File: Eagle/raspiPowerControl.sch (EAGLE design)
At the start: 10 parts, among them Q1 FDN360P, T1 BC847

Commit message: Update Eagle
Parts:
- added C3: 100n, rcl:C-EUC0805
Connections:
- net +5V: now also C3.2
- net GND: now also C3.1
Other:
- moved on the sheet: +5V, GND, R1
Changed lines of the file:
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@@
 <part name="C1" library="rcl" library_urn="urn:adsk.eagle:library:334" deviceset="C-EU" device="C0805" package3d_urn="urn:adsk.eagle:package:23617/2" value="1u"/>
 <part name="GND4" library="supply1" library_urn="urn:adsk.eagle:library:371" deviceset="GND" device=""/>
+<part name="C3" library="rcl" library_urn="urn:adsk.eagle:library:334" deviceset="C-EU" device="C0805" package3d_urn="urn:adsk.eagle:package:23617/2" value="100n"/>
+<part name="GND5" library="supply1" library_urn="urn:adsk.eagle:library:371" deviceset="GND" device=""/>
 </parts>
 <sheets>
@@
 </instance>
 <instance part="T1" gate="G$1" x="60.96" y="48.26" smashed="yes">
-<attribute name="NAME" x="50.8" y="55.88" size="1.778" layer="95"/>
-<attribute name="VALUE" x="50.8" y="53.34" size="1.778" layer="96"/>
+<attribute name="NAME" x="62.992" y="55.88" size="1.778" layer="95"/>
+<attribute name="VALUE" x="55.372" y="53.34" size="1.778" layer="96"/>
 </instance>
 <instance part="Q1" gate="G$1" x="73.66" y="68.58" smashed="yes" rot="R90">
@@
 <attribute name="VALUE" x="121.92" y="5.08" size="1.778" layer="96"/>
 </instance>
-<instance part="R1" gate="G$1" x="45.72" y="48.26" smashed="yes">
-<attribute name="NAME" x="41.91" y="49.7586" size="1.778" layer="95"/>
-<attribute name="VALUE" x="41.91" y="44.958" size="1.778" layer="96"/>
+<instance part="R1" gate="G$1" x="50.8" y="48.26" smashed="yes">
+<attribute name="NAME" x="46.99" y="49.7586" size="1.778" layer="95"/>
+<attribute name="VALUE" x="46.99" y="44.958" size="1.778" layer="96"/>
 </instance>
 <instance part="R2" gate="G$1" x="63.5" y="63.5" smashed="yes" rot="R90">
@@
 <attribute name="VALUE" x="60.96" y="2.54" size="1.778" layer="96"/>
 </instance>
-<instance part="+5V" gate="1" x="-7.62" y="71.12" smashed="yes" rot="R90">
-<attribute name="NAME" x="-10.541" y="69.85" size="1.778" layer="95" rot="R90"/>
+<instance part="+5V" gate="1" x="4.572" y="71.12" smashed="yes" rot="R90">
+<attribute name="NAME" x="1.651" y="69.85" size="1.778" layer="95" rot="R90"/>
 </instance>
-<instance part="GND" gate="1" x="-7.62" y="63.5" smashed="yes" rot="R90">
-<attribute name="NAME" x="-10.541" y="62.23" size="1.778" layer="95" rot="R90"/>
+<instance part="GND" gate="1" x="4.572" y="63.5" smashed="yes" rot="R90">
+<attribute name="NAME" x="1.651" y="62.23" size="1.778" layer="95" rot="R90"/>
 </instance>
-<instance part="GND3" gate="1" x="-2.54" y="53.34" smashed="yes">
-<attribute name="VALUE" x="-5.08" y="50.8" size="1.778" layer="96"/>
+<instance part="GND3" gate="1" x="9.652" y="53.34" smashed="yes">
+<attribute name="VALUE" x="7.112" y="50.8" size="1.778" layer="96"/>
 </instance>
 <instance part="LED1" gate="G$1" x="35.56" y="63.5" smashed="yes">
@@
 <instance part="GND4" gate="1" x="35.56" y="5.08" smashed="yes">
 <attribute name="VALUE" x="33.02" y="2.54" size="1.778" layer="96"/>
+</instance>
+<instance part="C3" gate="G$1" x="17.272" y="63.5" smashed="yes" rot="R180">
+<attribute name="NAME" x="15.748" y="63.119" size="1.778" layer="95" rot="R180"/>
+<attribute name="VALUE" x="15.748" y="68.199" size="1.778" layer="96" rot="R180"/>
+</instance>
+<instance part="GND5" gate="1" x="17.272" y="53.34" smashed="yes">
+<attribute name="VALUE" x="14.732" y="50.8" size="1.778" layer="96"/>
 </instance>
 </instances>
@@
 <pinref part="GND" gate="1" pin="MP"/>
 <pinref part="GND3" gate="1" pin="GND"/>
-<wire x1="-5.08" y1="63.5" x2="-2.54" y2="63.5" width="0.1524" layer="91"/>
-<wire x1="-2.54" y1="63.5" x2="-2.54" y2="55.88" width="0.1524" layer="91"/>
+<wire x1="7.112" y1="63.5" x2="9.652" y2="63.5" width="0.1524" layer="91"/>
+<wire x1="9.652" y1="63.5" x2="9.652" y2="55.88" width="0.1524" layer="91"/>
 </segment>
 <segment>
@@
 <pinref part="C1" gate="G$1" pin="1"/>
 <wire x1="35.56" y1="7.62" x2="35.56" y2="10.16" width="0.1524" layer="91"/>
+</segment>
+<segment>
+<pinref part="C3" gate="G$1" pin="1"/>
+<pinref part="GND5" gate="1" pin="GND"/>
+<wire x1="17.272" y1="60.96" x2="17.272" y2="55.88" width="0.1524" layer="91"/>
 </segment>
 </net>
@@
 <wire x1="63.5" y1="71.12" x2="68.58" y2="71.12" width="0.1524" layer="91"/>
 <pinref part="+5V" gate="1" pin="MP"/>
-<wire x1="-5.08" y1="71.12" x2="35.56" y2="71.12" width="0.1524" layer="91"/>
 <junction x="63.5" y="71.12"/>
+<label x="37.592" y="73.66" size="1.778" layer="95" rot="R180"/>
+<wire x1="7.112" y1="71.12" x2="17.272" y2="71.12" width="0.1524" layer="91"/>
+<wire x1="17.272" y1="71.12" x2="35.56" y2="71.12" width="0.1524" layer="91"/>
+<pinref part="C3" gate="G$1" pin="2"/>
+<wire x1="35.56" y1="71.12" x2="63.5" y2="71.12" width="0.1524" layer="91"/>
+<wire x1="17.272" y1="71.12" x2="17.272" y2="68.58" width="0.1524" layer="91"/>
+<junction x="17.272" y="71.12"/>
 <pinref part="LED1" gate="G$1" pin="A"/>
-<wire x1="35.56" y1="71.12" x2="63.5" y2="71.12" width="0.1524" layer="91"/>
 <wire x1="35.56" y1="66.04" x2="35.56" y2="71.12" width="0.1524" layer="91"/>
 <junction x="35.56" y="71.12"/>
-<label x="25.4" y="73.66" size="1.778" layer="95" rot="R180"/>
 </segment>
 </net>
@@
 <pinref part="R1" gate="G$1" pin="2"/>
 <pinref part="T1" gate="G$1" pin="B"/>
-<wire x1="50.8" y1="48.26" x2="58.42" y2="48.26" width="0.1524" layer="91"/>
+<wire x1="55.88" y1="48.26" x2="58.42" y2="48.26" width="0.1524" layer="91"/>
 </segment>
 </net>
@@
 <pinref part="R1" gate="G$1" pin="1"/>
 <wire x1="15.24" y1="33.02" x2="15.24" y2="48.26" width="0.1524" layer="91"/>
-<wire x1="15.24" y1="48.26" x2="40.64" y2="48.26" width="0.1524" layer="91"/>
+<wire x1="15.24" y1="48.26" x2="45.72" y2="48.26" width="0.1524" layer="91"/>
 </segment>
 </net>
 <net name="PWR" class="0">
 <segment>
-<pinref part="LED1" gate="G$1" pin="C"/>
-<wire x1="35.56" y1="58.42" x2="35.56" y2="60.96" width="0.1524" layer="91"/>
-<wire x1="35.56" y1="58.42" x2="35.56" y2="20.32" width="0.1524" layer="91"/>
 <pinref part="U$1" gate="G$1" pin="5V"/>
 <wire x1="35.56" y1="20.32" x2="20.32" y2="20.32" width="0.1524" layer="91"/>
 <pinref part="C1" gate="G$1" pin="2"/>
 <wire x1="35.56" y1="17.78" x2="35.56" y2="20.32" width="0.1524" layer="91"/>
+<wire x1="35.56" y1="55.88" x2="35.56" y2="20.32" width="0.1524" layer="91"/>
 <junction x="35.56" y="20.32"/>
+<wire x1="35.56" y1="55.88" x2="55.88" y2="55.88" width="0.1524" layer="91"/>
+<pinref part="LED1" gate="G$1" pin="C"/>
+<wire x1="35.56" y1="55.88" x2="35.56" y2="58.42" width="0.1524" layer="91"/>
+<junction x="35.56" y="55.88"/>
 </segment>
 </net>

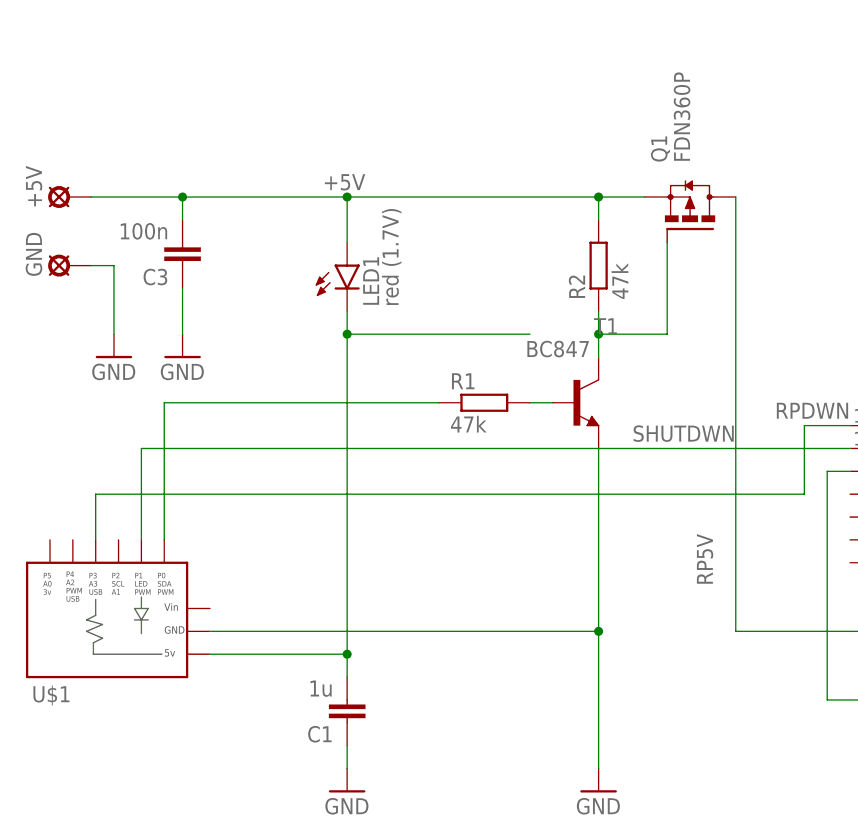
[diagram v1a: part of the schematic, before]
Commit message: Add regulator to design
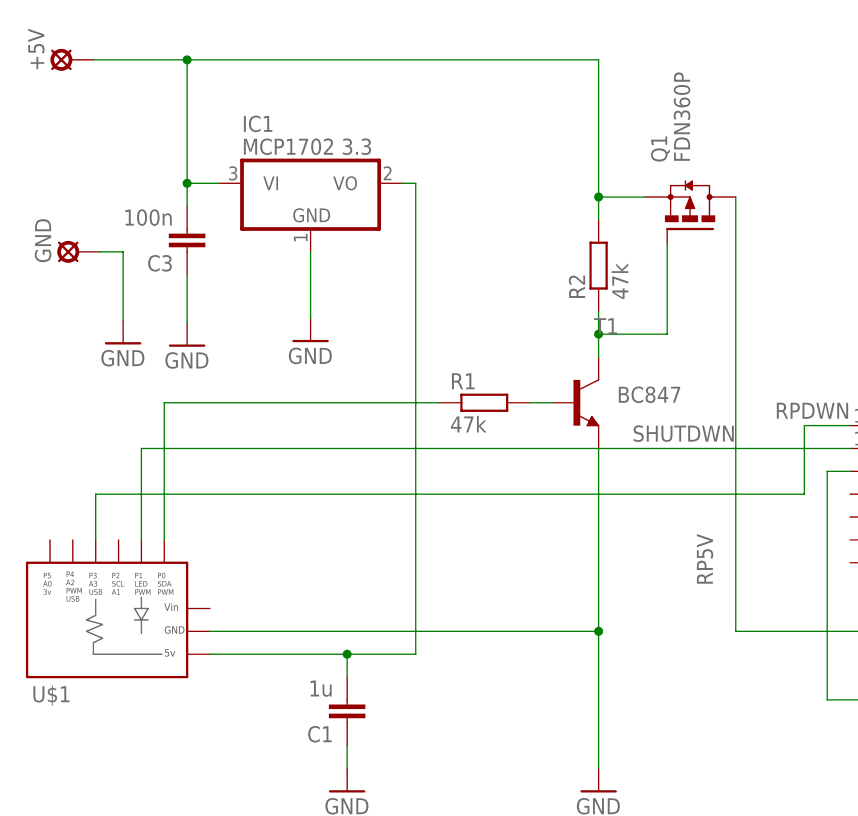
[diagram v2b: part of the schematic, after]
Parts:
- removed LED1: red (1.7V), led:LEDSMT1206
- added IC1: MCP1702 3.3, linear:MCP1703CB
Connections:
- removed net +5V: +5V.MP, C3.2, LED1.A, Q1.S, R2.2
- new net N$2: +5V.MP, C3.2, IC1.VI, Q1.S, R2.2
- net GND: now also IC1.GND
- net PWR: now also IC1.VO; no longer LED1.C
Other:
- moved on the sheet: +5V, C3, GND
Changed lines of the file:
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@@
 <part name="GND" library="solpad" library_urn="urn:adsk.eagle:library:364" deviceset="SE14" device="" package3d_urn="urn:adsk.eagle:package:26504/1"/>
 <part name="GND3" library="supply1" library_urn="urn:adsk.eagle:library:371" deviceset="GND" device=""/>
-<part name="LED1" library="led" library_urn="urn:adsk.eagle:library:259" deviceset="LED" device="SMT1206" package3d_urn="urn:adsk.eagle:package:15796/2" value="red (1.7V)"/>
 <part name="C1" library="rcl" library_urn="urn:adsk.eagle:library:334" deviceset="C-EU" device="C0805" package3d_urn="urn:adsk.eagle:package:23617/2" value="1u"/>
 <part name="GND4" library="supply1" library_urn="urn:adsk.eagle:library:371" deviceset="GND" device=""/>
 <part name="C3" library="rcl" library_urn="urn:adsk.eagle:library:334" deviceset="C-EU" device="C0805" package3d_urn="urn:adsk.eagle:package:23617/2" value="100n"/>
 <part name="GND5" library="supply1" library_urn="urn:adsk.eagle:library:371" deviceset="GND" device=""/>
+<part name="IC1" library="linear" library_urn="urn:adsk.eagle:library:262" deviceset="MCP1703" device="CB" package3d_urn="urn:adsk.eagle:package:16489/2" value="MCP1702 3.3"/>
+<part name="GND6" library="supply1" library_urn="urn:adsk.eagle:library:371" deviceset="GND" device=""/>
 </parts>
 <sheets>
@@
 <instance part="T1" gate="G$1" x="60.96" y="48.26" smashed="yes">
 <attribute name="NAME" x="62.992" y="55.88" size="1.778" layer="95"/>
-<attribute name="VALUE" x="55.372" y="53.34" size="1.778" layer="96"/>
+<attribute name="VALUE" x="65.532" y="48.26" size="1.778" layer="96"/>
 </instance>
 <instance part="Q1" gate="G$1" x="73.66" y="68.58" smashed="yes" rot="R90">
@@
 <attribute name="VALUE" x="60.96" y="2.54" size="1.778" layer="96"/>
 </instance>
-<instance part="+5V" gate="1" x="4.572" y="71.12" smashed="yes" rot="R90">
-<attribute name="NAME" x="1.651" y="69.85" size="1.778" layer="95" rot="R90"/>
-</instance>
-<instance part="GND" gate="1" x="4.572" y="63.5" smashed="yes" rot="R90">
-<attribute name="NAME" x="1.651" y="62.23" size="1.778" layer="95" rot="R90"/>
-</instance>
-<instance part="GND3" gate="1" x="9.652" y="53.34" smashed="yes">
-<attribute name="VALUE" x="7.112" y="50.8" size="1.778" layer="96"/>
-</instance>
-<instance part="LED1" gate="G$1" x="35.56" y="63.5" smashed="yes">
-<attribute name="NAME" x="39.116" y="58.928" size="1.778" layer="95" rot="R90"/>
-<attribute name="VALUE" x="41.275" y="58.928" size="1.778" layer="96" rot="R90"/>
+<instance part="+5V" gate="1" x="4.826" y="86.36" smashed="yes" rot="R90">
+<attribute name="NAME" x="1.905" y="85.09" size="1.778" layer="95" rot="R90"/>
+</instance>
+<instance part="GND" gate="1" x="5.588" y="65.024" smashed="yes" rot="R90">
+<attribute name="NAME" x="2.667" y="63.754" size="1.778" layer="95" rot="R90"/>
+</instance>
+<instance part="GND3" gate="1" x="10.668" y="54.864" smashed="yes">
+<attribute name="VALUE" x="8.128" y="52.324" size="1.778" layer="96"/>
 </instance>
 <instance part="C1" gate="G$1" x="35.56" y="12.7" smashed="yes" rot="R180">
@@
 <attribute name="VALUE" x="33.02" y="2.54" size="1.778" layer="96"/>
 </instance>
-<instance part="C3" gate="G$1" x="17.272" y="63.5" smashed="yes" rot="R180">
-<attribute name="NAME" x="15.748" y="63.119" size="1.778" layer="95" rot="R180"/>
-<attribute name="VALUE" x="15.748" y="68.199" size="1.778" layer="96" rot="R180"/>
-</instance>
-<instance part="GND5" gate="1" x="17.272" y="53.34" smashed="yes">
-<attribute name="VALUE" x="14.732" y="50.8" size="1.778" layer="96"/>
+<instance part="C3" gate="G$1" x="17.78" y="65.024" smashed="yes" rot="R180">
+<attribute name="NAME" x="16.256" y="64.643" size="1.778" layer="95" rot="R180"/>
+<attribute name="VALUE" x="16.256" y="69.723" size="1.778" layer="96" rot="R180"/>
+</instance>
+<instance part="GND5" gate="1" x="17.78" y="54.61" smashed="yes">
+<attribute name="VALUE" x="15.24" y="52.07" size="1.778" layer="96"/>
+</instance>
+<instance part="IC1" gate="G$1" x="31.496" y="72.644" smashed="yes">
+<attribute name="NAME" x="23.876" y="78.359" size="1.778" layer="95"/>
+<attribute name="VALUE" x="23.876" y="75.819" size="1.778" layer="96"/>
+</instance>
+<instance part="GND6" gate="1" x="31.496" y="55.118" smashed="yes">
+<attribute name="VALUE" x="28.956" y="52.578" size="1.778" layer="96"/>
 </instance>
 </instances>
@@
 <pinref part="GND" gate="1" pin="MP"/>
 <pinref part="GND3" gate="1" pin="GND"/>
-<wire x1="7.112" y1="63.5" x2="9.652" y2="63.5" width="0.1524" layer="91"/>
-<wire x1="9.652" y1="63.5" x2="9.652" y2="55.88" width="0.1524" layer="91"/>
+<wire x1="8.128" y1="65.024" x2="10.668" y2="65.024" width="0.1524" layer="91"/>
+<wire x1="10.668" y1="65.024" x2="10.668" y2="57.404" width="0.1524" layer="91"/>
 </segment>
 <segment>
@@
 </segment>
 <segment>
+<pinref part="GND5" gate="1" pin="GND"/>
 <pinref part="C3" gate="G$1" pin="1"/>
-<pinref part="GND5" gate="1" pin="GND"/>
-<wire x1="17.272" y1="60.96" x2="17.272" y2="55.88" width="0.1524" layer="91"/>
-</segment>
-</net>
-<net name="+5V" class="0">
-<segment>
-<pinref part="R2" gate="G$1" pin="2"/>
-<wire x1="63.5" y1="68.58" x2="63.5" y2="71.12" width="0.1524" layer="91"/>
-<pinref part="Q1" gate="G$1" pin="S"/>
-<wire x1="63.5" y1="71.12" x2="68.58" y2="71.12" width="0.1524" layer="91"/>
-<pinref part="+5V" gate="1" pin="MP"/>
-<junction x="63.5" y="71.12"/>
-<label x="37.592" y="73.66" size="1.778" layer="95" rot="R180"/>
-<wire x1="7.112" y1="71.12" x2="17.272" y2="71.12" width="0.1524" layer="91"/>
-<wire x1="17.272" y1="71.12" x2="35.56" y2="71.12" width="0.1524" layer="91"/>
-<pinref part="C3" gate="G$1" pin="2"/>
-<wire x1="35.56" y1="71.12" x2="63.5" y2="71.12" width="0.1524" layer="91"/>
-<wire x1="17.272" y1="71.12" x2="17.272" y2="68.58" width="0.1524" layer="91"/>
-<junction x="17.272" y="71.12"/>
-<pinref part="LED1" gate="G$1" pin="A"/>
-<wire x1="35.56" y1="66.04" x2="35.56" y2="71.12" width="0.1524" layer="91"/>
-<junction x="35.56" y="71.12"/>
+<wire x1="17.78" y1="57.15" x2="17.78" y2="62.484" width="0.1524" layer="91"/>
+</segment>
+<segment>
+<pinref part="GND6" gate="1" pin="GND"/>
+<pinref part="IC1" gate="G$1" pin="GND"/>
+<wire x1="31.496" y1="57.658" x2="31.496" y2="65.024" width="0.1524" layer="91"/>
 </segment>
 </net>
@@
 <pinref part="C1" gate="G$1" pin="2"/>
 <wire x1="35.56" y1="17.78" x2="35.56" y2="20.32" width="0.1524" layer="91"/>
-<wire x1="35.56" y1="55.88" x2="35.56" y2="20.32" width="0.1524" layer="91"/>
+<wire x1="43.18" y1="20.32" x2="35.56" y2="20.32" width="0.1524" layer="91"/>
 <junction x="35.56" y="20.32"/>
-<wire x1="35.56" y1="55.88" x2="55.88" y2="55.88" width="0.1524" layer="91"/>
-<pinref part="LED1" gate="G$1" pin="C"/>
-<wire x1="35.56" y1="55.88" x2="35.56" y2="58.42" width="0.1524" layer="91"/>
-<junction x="35.56" y="55.88"/>
+<pinref part="IC1" gate="G$1" pin="VO"/>
+<wire x1="41.656" y1="72.644" x2="43.18" y2="72.644" width="0.1524" layer="91"/>
+<wire x1="43.18" y1="72.644" x2="43.18" y2="20.32" width="0.1524" layer="91"/>
 </segment>
 </net>
@@
 </segment>
 </net>
+<net name="N$2" class="0">
+<segment>
+<pinref part="C3" gate="G$1" pin="2"/>
+<wire x1="17.78" y1="70.104" x2="17.78" y2="72.644" width="0.1524" layer="91"/>
+<pinref part="+5V" gate="1" pin="MP"/>
+<wire x1="17.78" y1="72.644" x2="17.78" y2="86.36" width="0.1524" layer="91"/>
+<wire x1="7.366" y1="86.36" x2="17.78" y2="86.36" width="0.1524" layer="91"/>
+<pinref part="R2" gate="G$1" pin="2"/>
+<wire x1="63.5" y1="68.58" x2="63.5" y2="71.12" width="0.1524" layer="91"/>
+<pinref part="Q1" gate="G$1" pin="S"/>
+<wire x1="63.5" y1="71.12" x2="68.58" y2="71.12" width="0.1524" layer="91"/>
+<junction x="63.5" y="71.12"/>
+<wire x1="63.5" y1="86.36" x2="63.5" y2="71.12" width="0.1524" layer="91"/>
+<wire x1="17.78" y1="86.36" x2="63.5" y2="86.36" width="0.1524" layer="91"/>
+<junction x="17.78" y="86.36"/>
+<pinref part="IC1" gate="G$1" pin="VI"/>
+<wire x1="21.336" y1="72.644" x2="17.78" y2="72.644" width="0.1524" layer="91"/>
+<junction x="17.78" y="72.644"/>
+</segment>
+</net>

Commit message: Add DC/DC converter to design
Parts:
- removed +5V, GND: SE14, solpad:SE14
- added D1: BAS40, diode:BAS40
- added J1: (no value), con-amp:MTA03-100
- added J2: (no value), con-amp:MTA02-100
- added MP1584: DCDC-MINI, raspiPowerControl:DCDC-MINI
- added USB1: MOLEX-47346-0001, usb_con-update:MOLEX-47346-0001
- IC1: value MCP1702 3.3 -> MCP1702/3 3.3
- renumbered U$1 to ATTINY85
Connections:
- new net +12V: J2.1, MP1584.IN+@1, MP1584.IN+@2
- new net +5V: D1.A, MP1584.OUT+@1, MP1584.OUT+@2, Q1.S, R2.2, USB1.1
- new net N$1: C3.2, D1.C, IC1.VI
- new net N$6: ATTINY85.P4, J1.1
- net GND: now also J1.2, J2.2, MP1584.IN-@1, MP1584.IN-@2, MP1584.OUT-@1, MP1584.OUT-@2, USB1.5; no longer GND.MP
- net N$2: now also USB1.3, USB1.4; no longer +5V.MP, C3.2, IC1.VI, Q1.S, R2.2
- net PWR: now also J1.3

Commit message: Modified layout
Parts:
- removed ATTINY85: DIGISPARK, raspiPowerControl:DIGISPARK
- removed J1: (no value), con-amp:MTA03-100
- removed USB1: MOLEX-47346-0001, usb_con-update:MOLEX-47346-0001
- added BUT: button, con-avx:009176003
- added DIGISPARK: DIGISPARKDIGISPARK-SMD, raspiPowerControl:DIGISPARKDIGISPARK-SMD
- added P2: (no value), jumper:SJ2W
- added PWR=5V: (no value), jumper:SJ
- C3: value 100n -> 1u
- MP1584: value DCDC-MINI -> DCDC-MINIDCDC-MINI-SMD; device raspiPowerControl:DCDC-MINI -> raspiPowerControl:DCDC-MINIDCDC-MINI-SMD
- Q1: value FDN360P -> DMP3098
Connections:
- removed net +12V: J2.1, MP1584.IN+@1, MP1584.IN+@2
- removed net N$2: USB1.3, USB1.4
- removed net N$5: ATTINY85.P0, R1.1
- removed net N$6: ATTINY85.P4, J1.1
- new net 3V3: BUT.3, C1.2, DIGISPARK.5V, IC1.VO
- new net BUT2: BUT.2, P2.2
- new net BUT4: BUT.1, DIGISPARK.P4
- new net P2: DIGISPARK.P2, P2.3
- new net SWPWR: DIGISPARK.P0, R1.1
- net +5V: now also PWR=5V.1; no longer USB1.1
- net GND: now also DIGISPARK.GND, J2.1, P2.1; no longer ATTINY85.GND, J1.2, J2.2, USB1.5
- net PWR: now also J2.2, MP1584.IN+@1, MP1584.IN+@2, PWR=5V.2; no longer ATTINY85.5V, C1.2, IC1.VO, J1.3
- net RPDWN: now also DIGISPARK.P3; no longer ATTINY85.P3
- net SHUTDWN: now also DIGISPARK.P1; no longer ATTINY85.P1
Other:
- note added: "Powering: via PWR pads. Either 5V (no DC/DC) or higher voltage with a DC/DC converter (e.g. 12V in a car). The corresponding solder jumper has to be closed. The Digispark/ATTINY85 runs on 3.3V ! MOSFET: FDN360P, DMP3098, TSM3401, TSM260 Button: - Jumper allows to set middle pad to GND or P2 - Pin 3 provides 3.3V for a touch button"
- moved on the sheet: J2, MP1584
